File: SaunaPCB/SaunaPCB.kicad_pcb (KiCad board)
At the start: 2 copper layers, 41 parts, among them J200a1 KL2RM7.62, J200b1 KL3RM7.62, J201a1 KL2RM7.62, J201b1 KL3RM7.62, J202 KL3RM7.62, J203 KL2RM7.62, J3 KL2RM5.08, J4 KL2RM5.08, J5 KL2RM5.08, J6 KL2RM5.08, K200 Relais_SPDT_CO, K201 Relais_SPDT_CO, K202 Relais_SPDT_CO, K203 Relais_SPDT_CO, K204 Relais_SPDT_CO, K205 Relais_SPDT_CO, K206 Relais_SPDT_CO, U1 4N25, U2 4N25, U3 4N25

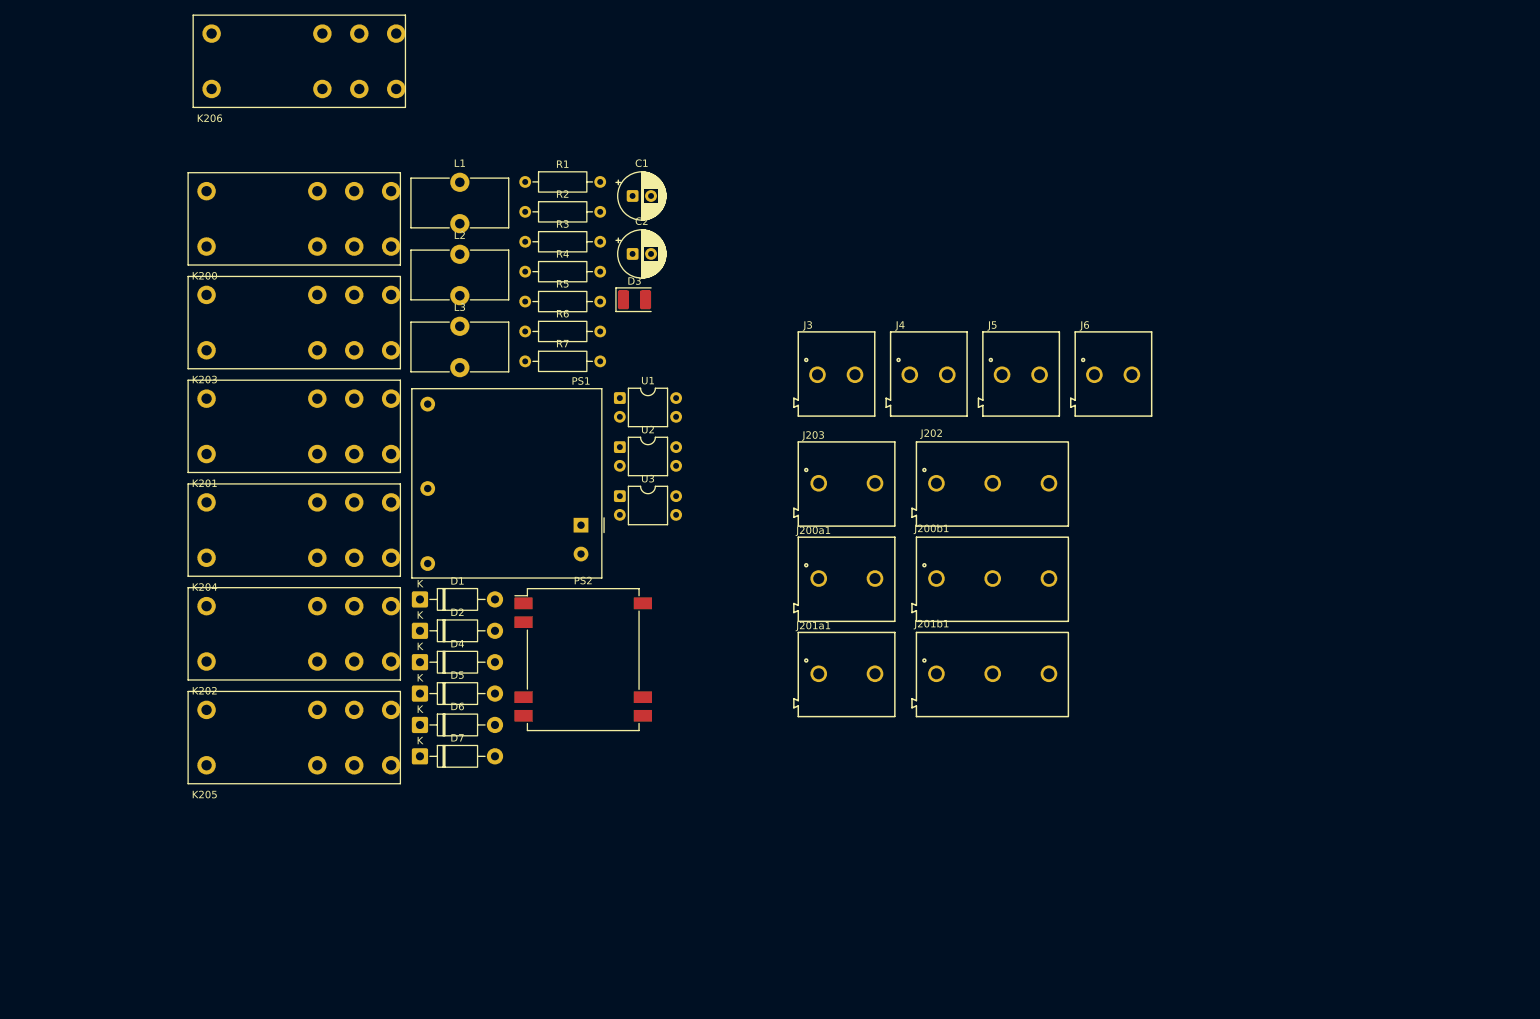
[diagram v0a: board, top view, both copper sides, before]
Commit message: Working on schematic and PCB -AC/DC and DC/DC converters with correct symbol and footprint now - rough placement of the power parts
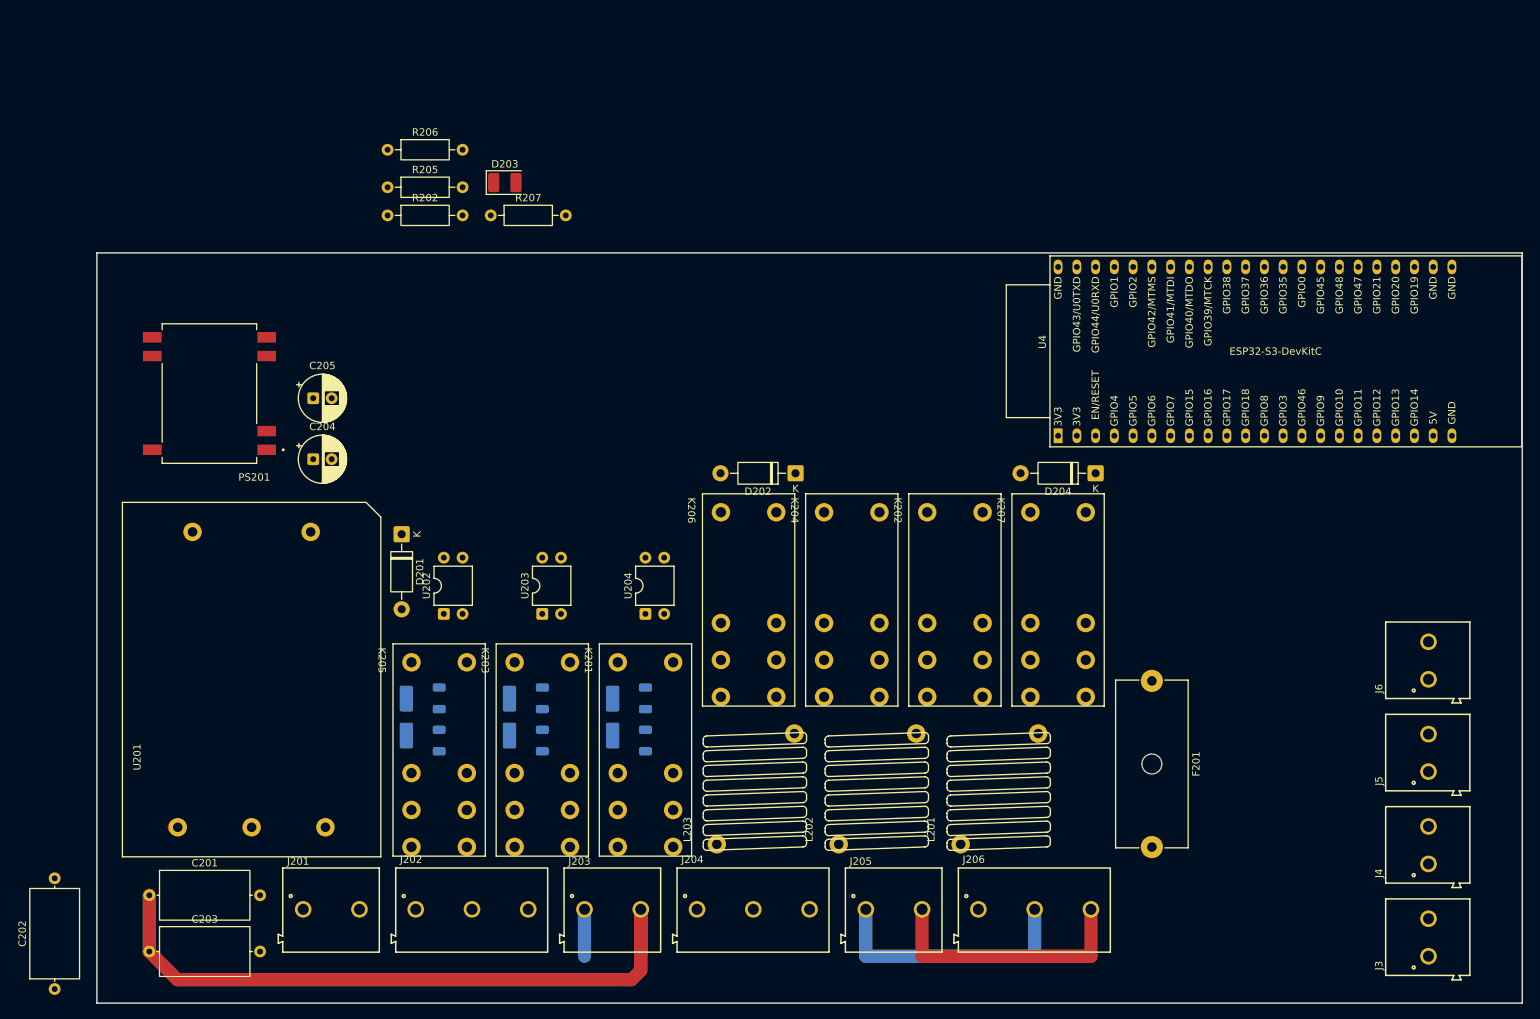
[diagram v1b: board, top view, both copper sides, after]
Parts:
- removed PS1: Mornsun 24V/230mA, Converter_ACDC:Converter_ACDC_RECOM_RAC05-xxSK_THT
- removed PS2: ISU0224S05, Converter_DCDC:Converter_DCDC_XP_POWER-ISU02_SMD
- added C201: 1nF, Capacitor_THT:C_Axial_L12.0mm_D6.5mm_P15.00mm_Horizontal, F.Cu at (80.8, 137.8)
- added C202: 33nF, Capacitor_THT:C_Axial_L12.0mm_D6.5mm_P15.00mm_Horizontal, F.Cu at (67.9, 150.5)
- added C203: 1nF, Capacitor_THT:C_Axial_L12.0mm_D6.5mm_P15.00mm_Horizontal, F.Cu at (80.8, 145.4)
- added F201: 1A/M, Fuse:Fuseholder_Cylinder-5x20mm_Schurter_0031_8201_Horizontal_Open, F.Cu at (216.5, 108.8)
- added PS201: RSH2-2405S_H3-R, DCDC:CONV_RSH2-2405S_H3-R, F.Cu at (88.9, 69.8)
- added R208: 100k, Resistor_SMD:R_1206_3216Metric, B.Cu at (148.0, 111.1)
- added R209: 100K, Resistor_SMD:R_1206_3216Metric, B.Cu at (134.0, 116.8)
- added R210: 100K, Resistor_SMD:R_1206_3216Metric, B.Cu at (120.0, 116.8)
- added U201: LHE05-20B24, Mornsun_ACDC:LHE05-20B24, F.Cu at (94.6, 108.6)
- added U4: ESP32-S3-DevKitC, Espreessif ESP32:ESP32-S3-DevKitC, F.Cu at (203.8, 75.6)
- D205: renamed from D5; footprint Diode_THT:D_DO-41_SOD81_P10.16mm_Horizontal -> Diode_SMD:D_SMA_Handsoldering; moved to B.Cu
- D206: renamed from D6; footprint Diode_THT:D_DO-41_SOD81_P10.16mm_Horizontal -> Diode_SMD:D_SMA_Handsoldering; moved to B.Cu
- D207: renamed from D7; footprint Diode_THT:D_DO-41_SOD81_P10.16mm_Horizontal -> Diode_SMD:D_SMA_Handsoldering; moved to B.Cu
- L201: renamed from L1; footprint Inductor_THT:L_Toroid_Vertical_L13.0mm_W6.5mm_P5.60mm -> SaunaProject:Current_Coil_15X14
- L202: renamed from L2; footprint Inductor_THT:L_Toroid_Vertical_L13.0mm_W6.5mm_P5.60mm -> SaunaProject:Current_Coil_15X14
- L203: renamed from L3; footprint Inductor_THT:L_Toroid_Vertical_L13.0mm_W6.5mm_P5.60mm -> SaunaProject:Current_Coil_15X14
- R201: renamed from R1; value 220K -> 100K; footprint Resistor_THT:R_Axial_DIN0207_L6.3mm_D2.5mm_P10.16mm_Horizontal -> Resistor_SMD:R_1206_3216Metric; moved to B.Cu
- R202: renamed from R2; value R -> 1K5
- R203: renamed from R3; value 220K -> 100K; footprint Resistor_THT:R_Axial_DIN0207_L6.3mm_D2.5mm_P10.16mm_Horizontal -> Resistor_SMD:R_1206_3216Metric; moved to B.Cu
- R204: renamed from R4; value 220K -> 100K; footprint Resistor_THT:R_Axial_DIN0207_L6.3mm_D2.5mm_P10.16mm_Horizontal -> Resistor_SMD:R_1206_3216Metric; moved to B.Cu
- moved K207 125.9 mm to (203.8, 98.4), turned to -90 degrees
- moved J3 110.6 mm to (254.0, 143.5), turned to 90 degrees
- moved L201 109.8 mm to (195.6, 123.4), turned to 90 degrees
- moved K202 96.7 mm to (189.9, 98.4), turned to -90 degrees
- moved D204 95.0 mm to (208.9, 80.6), turned to 180 degrees
- moved J4 93.0 mm to (254.0, 131.0), turned to 90 degrees
- moved L202 91.7 mm to (179.1, 123.4), turned to 90 degrees
- moved J201 90.6 mm to (105.4, 139.7)
- moved K201 86.4 mm to (148.0, 118.7), turned to -90 degrees
- moved J202 83.5 mm to (124.5, 139.7)
- moved R201 77.4 mm to (148.0, 116.8), turned to 90 degrees
- moved K204 75.6 mm to (175.9, 98.4), turned to -90 degrees
- moved J5 75.3 mm to (254.0, 118.5), turned to 90 degrees
- moved L203 74.2 mm to (162.6, 123.4), turned to 90 degrees
- moved K206 63.5 mm to (161.9, 98.4), turned to -90 degrees
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- renumbered C1 to C204, C2 to C205, D1 to D201, D2 to D202, D3 to D203, D4 to D204, J203 to J201, J200b1 to J202, J200a1 to J203, J201b1 to J204, J201a1 to J205, J202 to J206, K200 to K201, K203 to K202, K201 to K203, K202 to K205, K205 to K206, K206 to K207, R5 to R205, R6 to R206, R7 to R207, U1 to U202, U2 to U203, U3 to U204
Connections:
- net L1_SENSE renamed Net-(R205-Pad1)
- D207 pad 1: Net-(D7-K) -> Net-(D207-K)
- J201 pad 1: Net-(PS1-AC(L)) -> L1
- J201 pad 2: L1 -> Net-(U201-AC/L)
- J202 pad 1: L3 -> L1
- J202 pad 3: L1 -> L3
- J203 pad 1: PE -> N
- J203 pad 2: N -> PE
- J204 pad 1: /Power distribution part/L3_OUT -> /Power distribution part/L1_OUT
- J204 pad 3: /Power distribution part/L1_OUT -> /Power distribution part/L3_OUT
- J205 pad 1: PE -> N
- J205 pad 2: N -> PE
- J206 pad 1: PE -> Net-(F201-Pad2)
- J206 pad 3: Net-(J202-Pad3) -> PE
- K207 pad 14a: Net-(J202-Pad3) -> Net-(F201-Pad1)
- K207 pad 14b: Net-(J202-Pad3) -> Net-(F201-Pad1)
- R201 pad 2: Net-(D7-K) -> Net-(R201-Pad2)
- R203 pad 1: /Power distribution part/L2_SW -> Net-(R203-Pad1)
- R204 pad 1: /Power distribution part/L3_SW -> Net-(R204-Pad1)
- U204 pad 1: Net-(D7-K) -> Net-(D207-K)
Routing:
- net PE: track 0.00 -> 126.9 mm
- net N: track 0.00 -> 41.9 mm
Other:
- board outline added: 193 x 101.6 mm
- board text added: "Line power input"
- board text added: "Main switch"
- board text added: "Sauna light output"
- board text added: "Sauna oven output"

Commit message: Work on documnets and net classes
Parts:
- moved U4 73.2 mm to (263.5, 118.0), turned to 180 degrees
- moved J6 47.9 mm to (223.0, 142.5), turned to 180 degrees
- moved J5 30.3 mm to (235.5, 142.5), turned to 180 degrees
- moved J4 12.9 mm to (248.0, 142.5), turned to 180 degrees
- moved J3 6.62 mm to (260.5, 142.5), turned to 180 degrees
- moved F201 4.05 mm to (216.0, 104.8)
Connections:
- net Net-(F201-Pad1) renamed /Power distribution part/Light_Out
- net Net-(K202-Pad14a) renamed /Power distribution part/K202_Out
- net Net-(K204-Pad14a) renamed /Power distribution part/K204_Out
- net Net-(K206-Pad14a) renamed /Power distribution part/K206_Out
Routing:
- net /Power distribution part/L3_OUT: track 0.00 -> 24.1 mm
- net /Power distribution part/Light_Out: track 0.00 -> 20.4 mm
- net /Power distribution part/K202_Out: track 0.00 -> 18.4 mm
- net /Power distribution part/K204_Out: track 0.00 -> 16.2 mm
- net /Power distribution part/L2_OUT: track 0.00 -> 15.2 mm
- net /Power distribution part/K206_Out: track 0.00 -> 14.2 mm
- net /Power distribution part/L1_OUT: track 0.00 -> 9.92 mm
- net L1: track 0.00 -> 7.50 mm
- net /Power distribution part/L3_SW: track 0.00 -> 7.50 mm
- net /Power distribution part/L2_SW: track 0.00 -> 7.50 mm
- net /Power distribution part/L1_SW: track 0.00 -> 7.50 mm

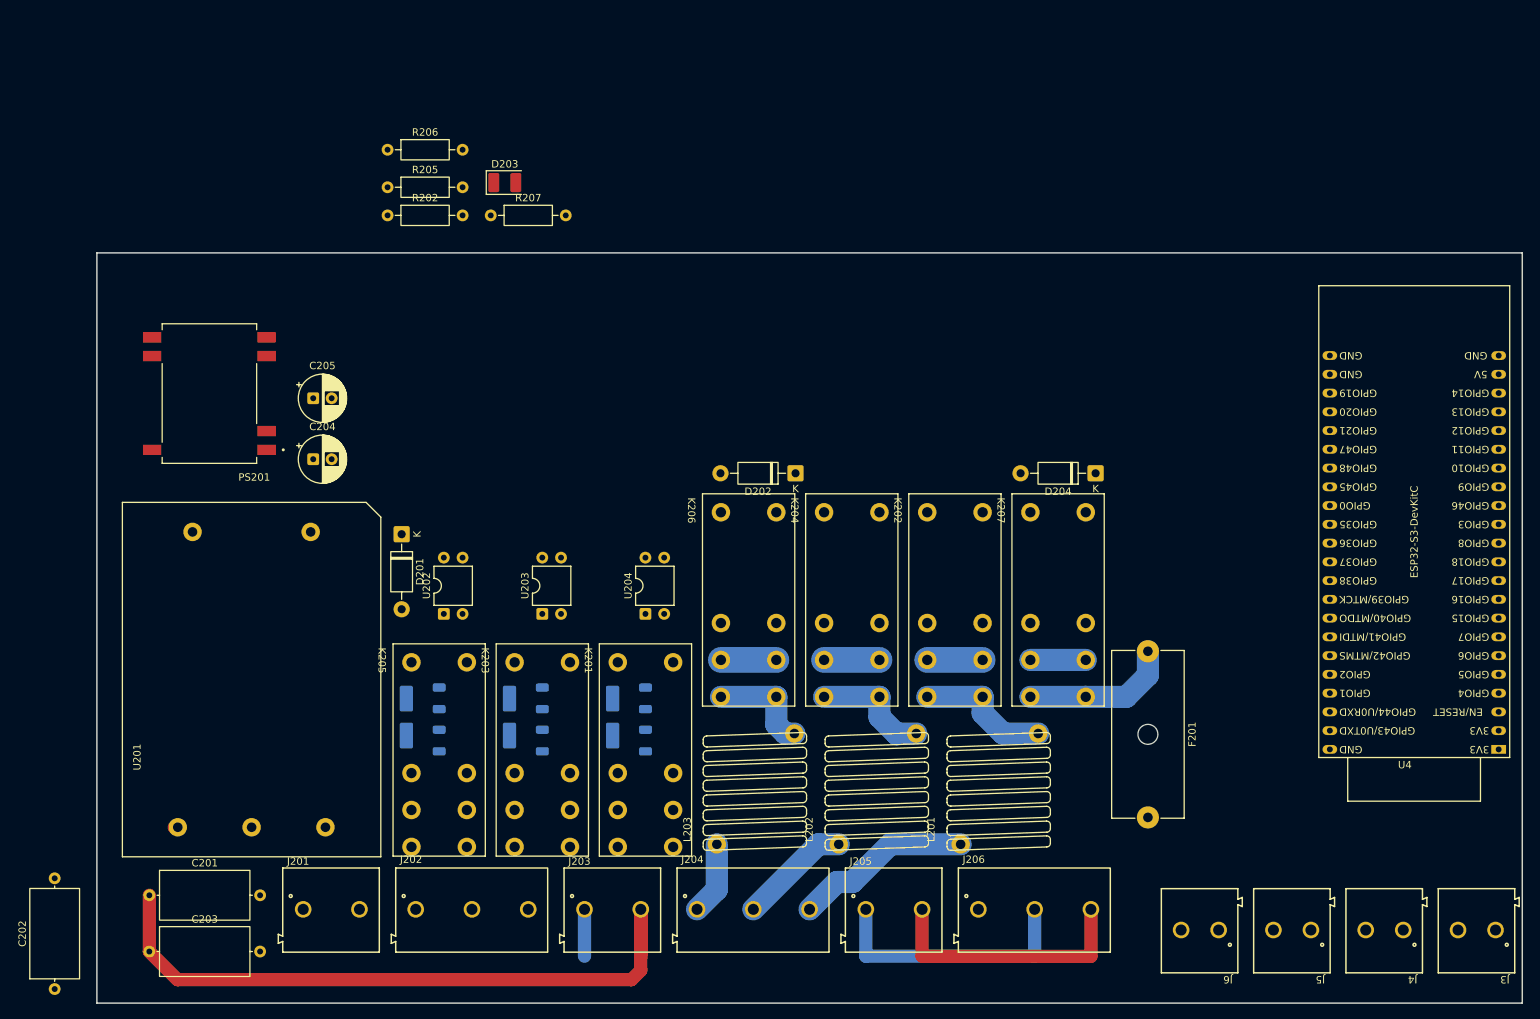
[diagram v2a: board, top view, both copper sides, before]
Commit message: Working on PCB placment optimisation Trace width and distance
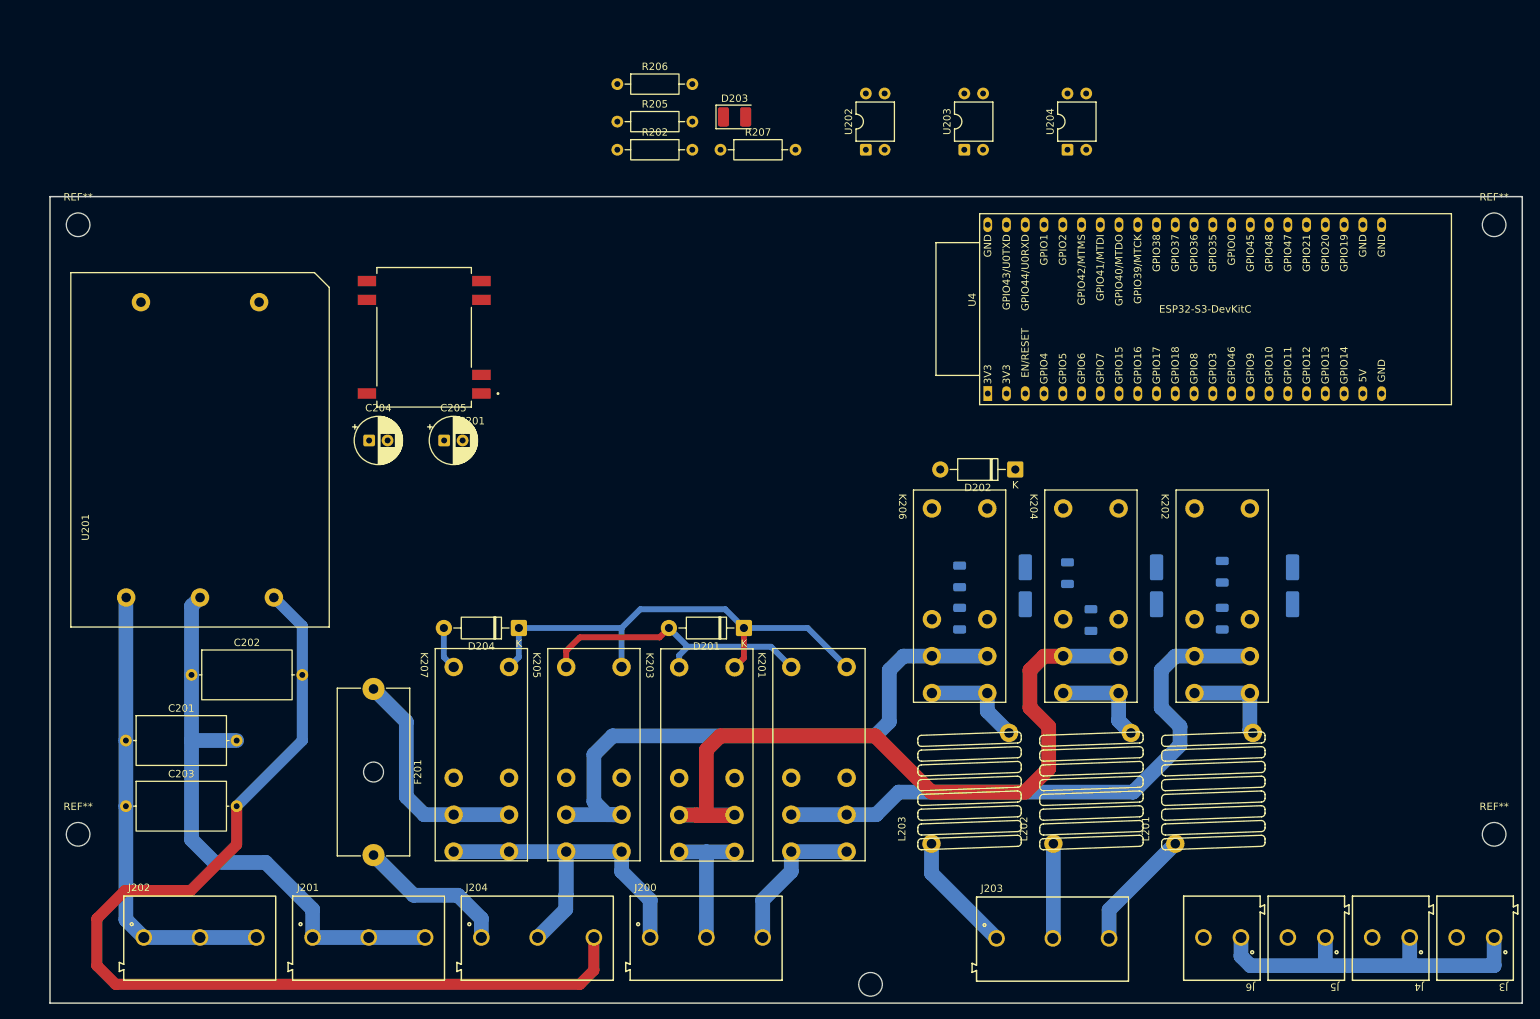
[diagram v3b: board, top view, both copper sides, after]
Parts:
- removed the J203 at (143.5, 139.7)
- removed J205: KL2RM7.62, MyConnectors:Terminal_Block_2_RM7.62
- added ?: , , F.Cu at (178.4, 149.9)
- added J202: KL3RM7.62, MyConnectors:Terminal_Block_3_RM7.62, F.Cu at (87.6, 143.5)
- added REF**: MountingHole_3.2mm_M3_DIN965, MountingHole:MountingHole_3.2mm_M3_DIN965, F.Cu at (71.1, 47.0)
- added REF**: MountingHole_3.2mm_M3_DIN965, MountingHole:MountingHole_3.2mm_M3_DIN965, F.Cu at (262.9, 47.0)
- added REF**: MountingHole_3.2mm_M3_DIN965, MountingHole:MountingHole_3.2mm_M3_DIN965, F.Cu at (71.1, 129.5)
- added REF**: MountingHole_3.2mm_M3_DIN965, MountingHole:MountingHole_3.2mm_M3_DIN965, F.Cu at (262.9, 129.5)
- J201: value KL2RM7.62 -> KL3RM7.62; footprint MyConnectors:Terminal_Block_2_RM7.62 -> MyConnectors:Terminal_Block_3_RM7.62
- moved F201 105.0 mm to (111.1, 109.9)
- moved D207 93.8 mm to (235.6, 95.9)
- moved D206 89.4 mm to (217.2, 95.9)
- moved D205 85.7 mm to (199.4, 95.9)
- moved U202 85.0 mm to (177.8, 36.8)
- moved U203 85.0 mm to (191.1, 36.8)
- moved U204 85.0 mm to (205.1, 36.8)
- moved U4 84.3 mm to (194.3, 69.8), turned to 90 degrees
- moved K207 80.9 mm to (125.7, 119.4)
- moved D204 80.9 mm to (130.8, 101.6)
- moved R208 80.0 mm to (226.1, 94.0)
- moved R201 79.8 mm to (226.1, 100.3)
- moved R209 76.1 mm to (208.3, 100.5)
- moved R203 73.1 mm to (205.1, 94.2)
- moved R204 72.4 mm to (190.5, 94.6)
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- renumbered J202 to J200, J204 to J203, J206 to J204
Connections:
- C202 pad 2: Net-(U201-AC/L) -> L1_ON
- C203 pad 2: Net-(U201-AC/L) -> L1_ON
- J201 pad 1: L1 -> N
- J201 pad 2: Net-(U201-AC/L) -> N
- J204 pad 2: N -> L1
- J204 pad 3: PE -> L1_ON
- K201 pad 11a: L3 -> /Power distribution part/L1_SW
- K201 pad 11b: L3 -> /Power distribution part/L1_SW
- K201 pad 14a: /Power distribution part/L1_SW -> L3
- K201 pad 14b: /Power distribution part/L1_SW -> L3
- K203 pad 11a: L2 -> /Power distribution part/L2_SW
- K203 pad 11b: L2 -> /Power distribution part/L2_SW
- K203 pad 14a: /Power distribution part/L2_SW -> L2
- K203 pad 14b: /Power distribution part/L2_SW -> L2
- K205 pad 11a: L1 -> /Power distribution part/L3_SW
- K205 pad 11b: L1 -> /Power distribution part/L3_SW
- K205 pad 14a: /Power distribution part/L3_SW -> L1
- K205 pad 14b: /Power distribution part/L3_SW -> L1
- K207 pad 11a: L1 -> /Power distribution part/Light_Out
- K207 pad 11b: L1 -> /Power distribution part/Light_Out
- K207 pad 14a: /Power distribution part/Light_Out -> L1
- K207 pad 14b: /Power distribution part/Light_Out -> L1
- U201 pad 1: Net-(U201-AC/L) -> L1_ON
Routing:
- net L1_ON: track 0.00 -> 141.8 mm
- net /Power distribution part/L2_SW: track 7.50 -> 98.9 mm
- net /Power distribution part/L3_SW: track 7.50 -> 82.4 mm
- net /Power distribution part/L1_SW: track 7.50 -> 80.5 mm
- net +24V: track 0.00 -> 65.6 mm
- net PE: track 126.9 -> 62.3 mm
- net GND: track 0.00 -> 48.8 mm
- net L1: track 7.50 -> 49.2 mm
- net Relais_1: track 0.00 -> 39.4 mm
- net N: track 41.9 -> 78.7 mm
- net L3: track 0.00 -> 20.7 mm
- net Net-(F201-Pad2): track 0.00 -> 20.7 mm
- net L2: track 0.00 -> 19.1 mm
- net /Power distribution part/Light_Out: track 20.4 -> 31.4 mm
- net /Power distribution part/L3_OUT: track 24.1 -> 16.5 mm
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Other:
- board size 193 x 101.6 mm -> 199.4 x 109.2 mm
- board text removed: "Line power input"
- board text removed: "Main switch"
- board text removed: "Sauna light output"
- board text removed: "Sauna oven output"
